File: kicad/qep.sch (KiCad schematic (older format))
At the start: 30 parts, among them J1101 tblock, U1101 SI8660BD, U1102 am26ls32a, U1103 am26ls32a, U1104 SI8660BD

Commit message: placing smmall capacitors and resistors nerar his group
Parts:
- added C1101, C1102, C1103, C1104, C1105, C1106: 100nF, servo:C_0603_1608Metric, symbol servo:Capacitor
- U1102, U1103: footprint Package_SO:SOIC-16_3.9x9.9mm_P1.27mm -> Package_SO:SOIC-16W_5.3x10.2mm_P1.27mm
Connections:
- net labels added: QEP2_A+_H, QEP2_A-_H, QEP2_B+_H, QEP2_B-_H, QEP2_I+_H, QEP2_I-_H, QEP2_S+_H, QEP2_S-_H
- wire segments 185 -> 197

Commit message: touting....
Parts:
- added JP1102: jumper, Jumper:SolderJumper-3_P1.3mm_Open_RoundedPad1.0x1.5mm, symbol servo:Jumper_3_Bridged12
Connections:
- net labels added: Earth
- wire segments 197 -> 202
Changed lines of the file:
@@
 L servo:GNDH #PWR?
 U 1 1 60472C0D
-P 5850 4450
+P 6200 4600
 AR Path="/5DDE8C5E/60472C0D" Ref="#PWR?"  Part="1"
 AR Path="/5E092156/60472C0D" Ref="#PWR0169"  Part="1"
-F 0 "#PWR0169" H 5850 4200 30  0001 C CNN
-F 1 "GNDH" H 5850 4300 20  0000 C CNN
-F 2 "" H 5850 4450 50  0001 C CNN
-F 3 "" H 5850 4450 50  0001 C CNN
-	1    5850 4450
+F 0 "#PWR0169" H 6200 4350 30  0001 C CNN
+F 1 "GNDH" H 6200 4450 20  0000 C CNN
+F 2 "" H 6200 4600 50  0001 C CNN
+F 3 "" H 6200 4600 50  0001 C CNN
+	1    6200 4600
 	-1   0    0    -1
 $EndComp
@@
 	-1   0    0    -1
 $EndComp
+$Comp
+L servo:Jumper_3_Bridged12 JP?
+U 1 1 5E2D8DCE
+P 5850 4550
+AR Path="/5E1BAEAA/5E2D8DCE" Ref="JP?"  Part="1"
+AR Path="/5E21534F/5E2D8DCE" Ref="JP?"  Part="1"
+AR Path="/5E092156/5E2D8DCE" Ref="JP1102"  Part="1"
+F 0 "JP1102" H 5850 4719 39  0000 C CNN
+F 1 "jumper" H 5850 4644 39  0000 C CNN
+F 2 "Jumper:SolderJumper-3_P1.3mm_Open_RoundedPad1.0x1.5mm" H 5650 4350 50  0001 C CNN
+F 3 "~" H 5750 4450 50  0001 C CNN
+	1    5850 4550
+	1    0    0    1
+$EndComp
+Wire Wire Line
+	6050 4550 6200 4550
+Wire Wire Line
+	6200 4550 6200 4600
+$Comp
+L servo:Earth #PWR?
+U 1 1 5E2D8DDD
+P 5500 4600
+AR Path="/5E21534F/5E2D8DDD" Ref="#PWR?"  Part="1"
+AR Path="/5E092156/5E2D8DDD" Ref="#PWR0224"  Part="1"
+F 0 "#PWR0224" H 5500 4350 20  0001 C CNN
+F 1 "Earth" H 5500 4435 39  0000 C CNN
+F 2 "" H 5500 4600 50  0001 C CNN
+F 3 "~" H 5500 4600 50  0001 C CNN
+	1    5500 4600
+	1    0    0    -1
+$EndComp
+Wire Wire Line
+	5650 4550 5500 4550
+Wire Wire Line
+	5500 4550 5500 4600
+Connection ~ 5500 4600
+Wire Wire Line
+	5500 4600 5500 4650
 $EndSCHEMATC

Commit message: moving ethernet connector to right and depopulate 15vh
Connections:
- net labels added: QEP1_A_H, QEP1_A_N_H, QEP1_A_P_H, QEP1_B_H, QEP1_B_N_H, QEP1_B_P_H, QEP1_I_H, QEP1_I_N_H, QEP1_I_P_H, QEP1_S_H, QEP1_S_N_H, QEP1_S_P_H, QEP2_A_H, QEP2_A_N_H, QEP2_A_P_H, QEP2_B_H, QEP2_B_N_H, QEP2_B_P_H, QEP2_I_H, QEP2_I_N_H, QEP2_I_P_H, QEP2_S_H, QEP2_S_N_H, QEP2_S_P_H
- net labels removed: QEP1_A+_H, QEP1_A-_H, QEP1_B+_H, QEP1_B-_H, QEP1_I+_H, QEP1_I-_H, QEP1_S+_H, QEP1_S-_H, QEP2_A+_H, QEP2_A-_H, QEP2_B+_H, QEP2_B-_H, QEP2_I+_H, QEP2_I-_H, QEP2_S+_H, QEP2_S-_H
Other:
- note added: "2x Isolated Idifferential incremental encoder interfase\n5v input A-B-I-S\n"
- note removed: "2x Isolated Idifferential ncremental encoder interfase\n5v input A-B-I-S\n"
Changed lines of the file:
@@
 $EndDescr
 Text Notes 2050 1450 0    197  ~ 39
-2x Isolated Idifferential ncremental encoder  interfase\n5v input A-B-I-S\n
+2x Isolated Idifferential incremental encoder  interfase\n5v input A-B-I-S\n
 Text Notes 3650 1650 0    20   ~ 4
 I left the input for two isolated incremental encoders.\nI left the 4 signals input plus two auxiliary output for eny porpous plus\n the ability to choose between 5 or 15vH
@@
 $EndComp
 Text Label 5400 3650 0    20   ~ 0
-QEP1_B+_H
+QEP1_B_P_H
 Text Label 5400 3750 0    20   ~ 0
-QEP1_B-_H
+QEP1_B_N_H
 Text GLabel 1100 3500 0    50   Input ~ 0
 QEP1_A
@@
 optional one to hi \nor/and one to low
 Text Label 6500 3350 2    20   ~ 0
-QEP2_A+_H
+QEP2_A_P_H
 Text Label 6500 3450 2    20   ~ 0
-QEP2_A-_H
+QEP2_A_N_H
 Text Label 6300 3650 2    20   ~ 0
-QEP2_B+_H
+QEP2_B_P_H
 Text Label 6300 3750 2    20   ~ 0
-QEP2_B-_H
+QEP2_B_N_H
 Text Label 6300 3850 2    20   ~ 0
-QEP2_I+_H
+QEP2_I_P_H
 Text Label 6300 3950 2    20   ~ 0
-QEP2_I-_H
+QEP2_I_N_H
 Text Label 6500 4150 2    20   ~ 0
-QEP2_S+_H
+QEP2_S_P_H
 Text Label 6500 4250 2    20   ~ 0
-QEP2_S-_H
+QEP2_S_N_H
 Text GLabel 10600 3500 2    50   Input ~ 0
 QEP2_A
@@
 optional one to hi \nor/and one to low
 Text Label 5200 3350 0    20   ~ 0
-QEP1_A+_H
+QEP1_A_P_H
 Text Label 5200 3450 0    20   ~ 0
-QEP1_A-_H
+QEP1_A_N_H
 Text Label 5400 3850 0    20   ~ 0
-QEP1_I+_H
+QEP1_I_P_H
 Text Label 5400 3950 0    20   ~ 0
-QEP1_I-_H
+QEP1_I_N_H
 Text Label 5200 4150 0    20   ~ 0
-QEP1_S+_H
+QEP1_S_P_H
 Text Label 5200 4250 0    20   ~ 0
-QEP1_S-_H
+QEP1_S_N_H
 $Comp
 L servo:GND #PWR?
@@
 Wire Wire Line
 	5500 4600 5500 4650
+Text Label 8900 3800 2    20   ~ 0
+QEP2_S_H
+Text Label 8900 3700 2    20   ~ 0
+QEP2_I_H
+Text Label 8900 3600 2    20   ~ 0
+QEP2_B_H
+Text Label 8900 3500 2    20   ~ 0
+QEP2_A_H
+Text Label 2700 3500 0    20   ~ 0
+QEP1_A_H
+Text Label 2700 3600 0    20   ~ 0
+QEP1_B_H
+Text Label 2700 3700 0    20   ~ 0
+QEP1_I_H
+Text Label 2700 3800 0    20   ~ 0
+QEP1_S_H
 $EndSCHEMATC

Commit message: roouting and more routing.... I think 4 layers WONT be enought
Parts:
- removed JP1101: jumper, Jumper:SolderJumper-3_P1.3mm_Open_RoundedPad1.0x1.5mm, symbol servo:Jumper_3_Bridged12
- added JP1101: jumper, servo:SolderJumper-2_P1.3mm_Open_RoundedPad1.0x1.5mm, symbol servo:jumper
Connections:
- net labels added: QEP_5VH
- net labels removed: 15VH
- wire segments 202 -> 201
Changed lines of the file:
@@
 	-1   0    0    -1
 $EndComp
-$Comp
-L servo:Jumper_3_Bridged12 JP?
-U 1 1 603AC069
-P 5850 3000
-AR Path="/5E1BAEAA/603AC069" Ref="JP?"  Part="1"
-AR Path="/5DE3DF56/603AC069" Ref="JP?"  Part="1"
-AR Path="/5E092156/603AC069" Ref="JP1101"  Part="1"
-F 0 "JP1101" H 5850 3169 39  0000 C CNN
-F 1 "jumper" H 5850 3094 39  0000 C CNN
-F 2 "Jumper:SolderJumper-3_P1.3mm_Open_RoundedPad1.0x1.5mm" H 5650 2800 50  0001 C CNN
-F 3 "~" H 5750 2900 50  0001 C CNN
-	1    5850 3000
-	-1   0    0    -1
-$EndComp
-$Comp
-L servo:15VH #PWR?
-U 1 1 603AC070
-P 5550 2950
-AR Path="/5E1BAEAA/603AC070" Ref="#PWR?"  Part="1"
-AR Path="/5DE3DF56/603AC070" Ref="#PWR?"  Part="1"
-AR Path="/5E092156/603AC070" Ref="#PWR0168"  Part="1"
-F 0 "#PWR0168" H 5550 2750 20  0001 C CNN
-F 1 "15VH" H 5550 3107 28  0000 C CNN
-F 2 "" H 5550 2950 50  0001 C CNN
-F 3 "" H 5550 2950 50  0001 C CNN
-	1    5550 2950
-	-1   0    0    -1
-$EndComp
-Wire Wire Line
-	5550 3000 5550 2950
-Wire Wire Line
-	5650 3000 5550 3000
 Wire Wire Line
 	6150 2950 6150 3000
@@
 Wire Wire Line
 	5600 3350 5600 3100
-Wire Wire Line
-	5600 3100 5850 3100
-Connection ~ 5850 3100
 $Comp
 L servo:GNDH #PWR?
@@
 Wire Wire Line
 	6100 3350 6100 3100
-Wire Wire Line
-	5850 3100 6100 3100
 Wire Wire Line
 	6300 3450 7450 3450
@@
 Text Label 2700 3800 0    20   ~ 0
 QEP1_S_H
+$Comp
+L servo:jumper JP?
+U 1 1 5E3094E2
+P 5950 3000
+AR Path="/5DD76B18/5E3094E2" Ref="JP?"  Part="1"
+AR Path="/5E092156/5E3094E2" Ref="JP1101"  Part="1"
+F 0 "JP1101" H 5950 3161 39  0000 C CNN
+F 1 "jumper" H 5950 3086 39  0000 C CNN
+F 2 "servo:SolderJumper-2_P1.3mm_Open_RoundedPad1.0x1.5mm" H 5850 2980 50  0001 C CNN
+F 3 "~" H 5950 3080 50  0001 C CNN
+	1    5950 3000
+	1    0    0    -1
+$EndComp
+Wire Wire Line
+	5600 3100 5850 3100
+Wire Wire Line
+	5850 3000 5850 3100
+Connection ~ 5850 3100
+Wire Wire Line
+	5850 3100 6100 3100
+Text Label 5650 3100 0    20   ~ 0
+QEP_5VH
 $EndSCHEMATC

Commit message: improvement...
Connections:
- net QEP_GND: now reaches J1101.10a (Pin_10a), J1101.10b (Pin_10b), JP1102.2 (C)
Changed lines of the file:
@@
 Text Label 5650 3100 0    20   ~ 0
 QEP_5VH
+Text Label 5950 4400 0    20   ~ 0
+QEP_GND
 $EndSCHEMATC

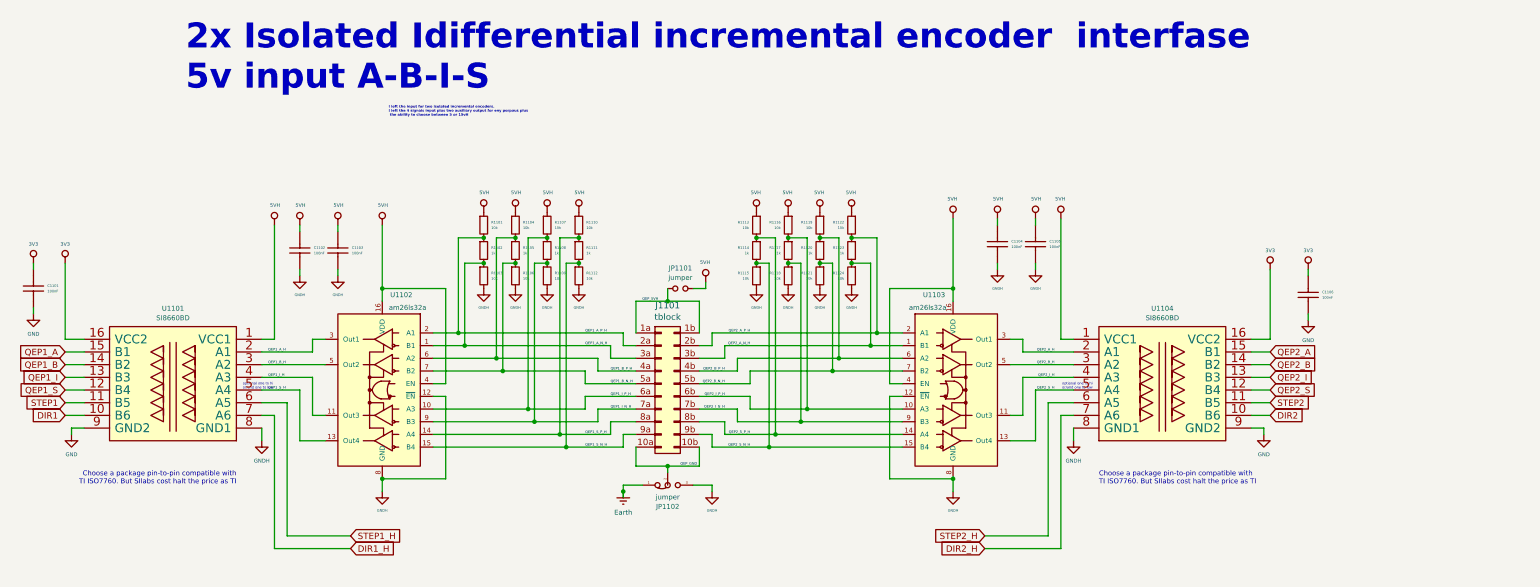
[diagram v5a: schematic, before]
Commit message: change in 5v interface scenario.. remove bridges
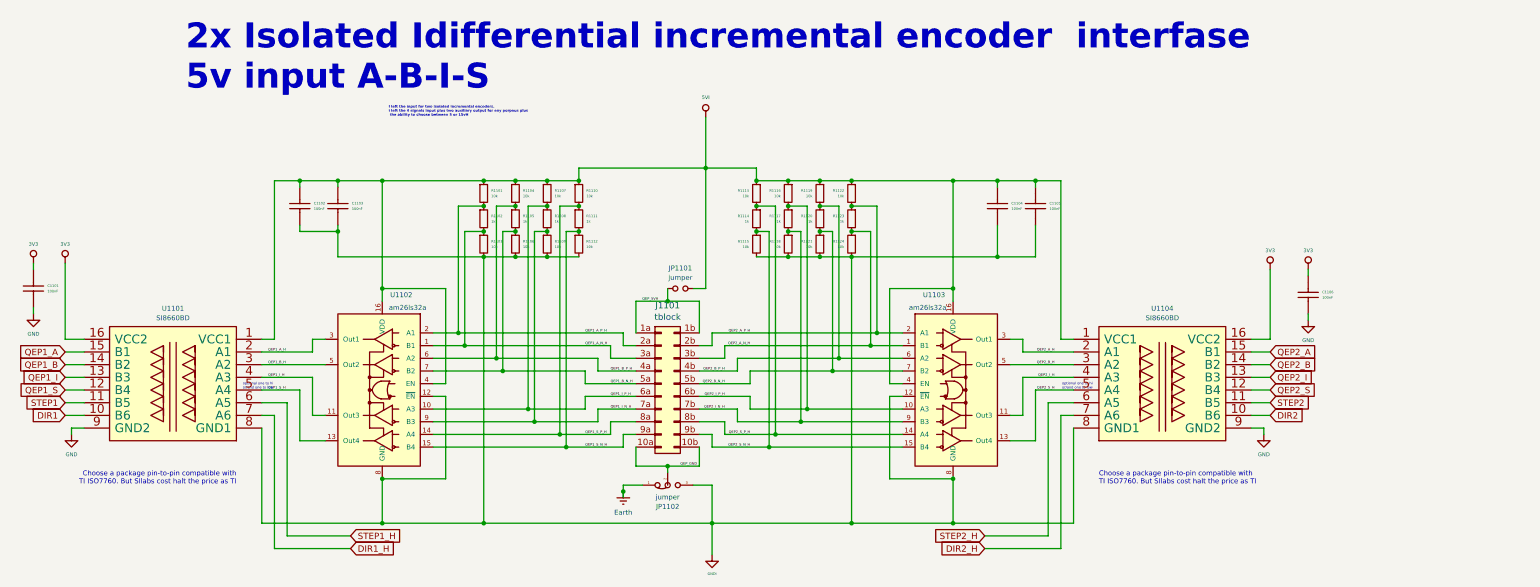
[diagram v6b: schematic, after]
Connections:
- net 5VH renamed 5VI
- net GNDH renamed GNDI
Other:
- moved on the sheet: C1102, C1103, C1104, C1105, R1101, R1102, R1103, R1104, R1105, R1106, R1107, R1108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

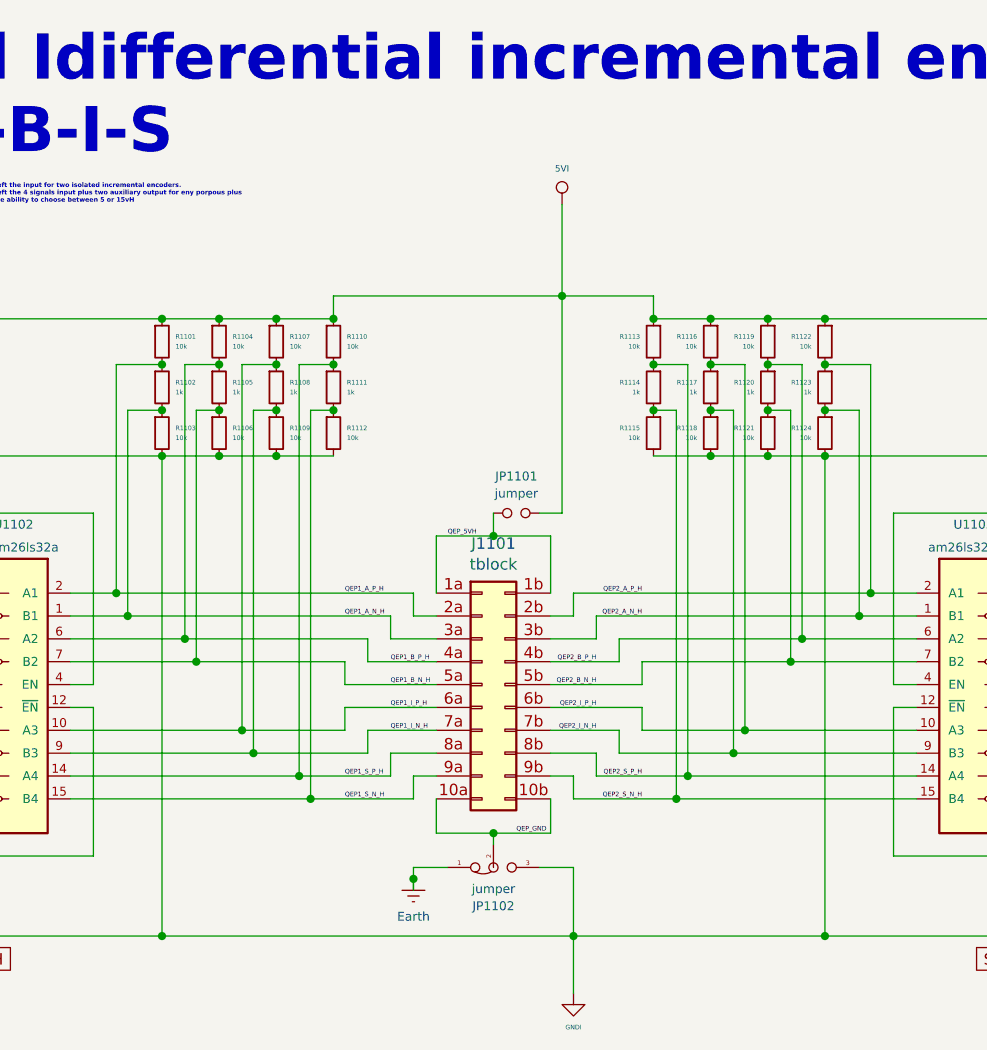
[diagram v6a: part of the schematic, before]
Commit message: added sloted holes everyware
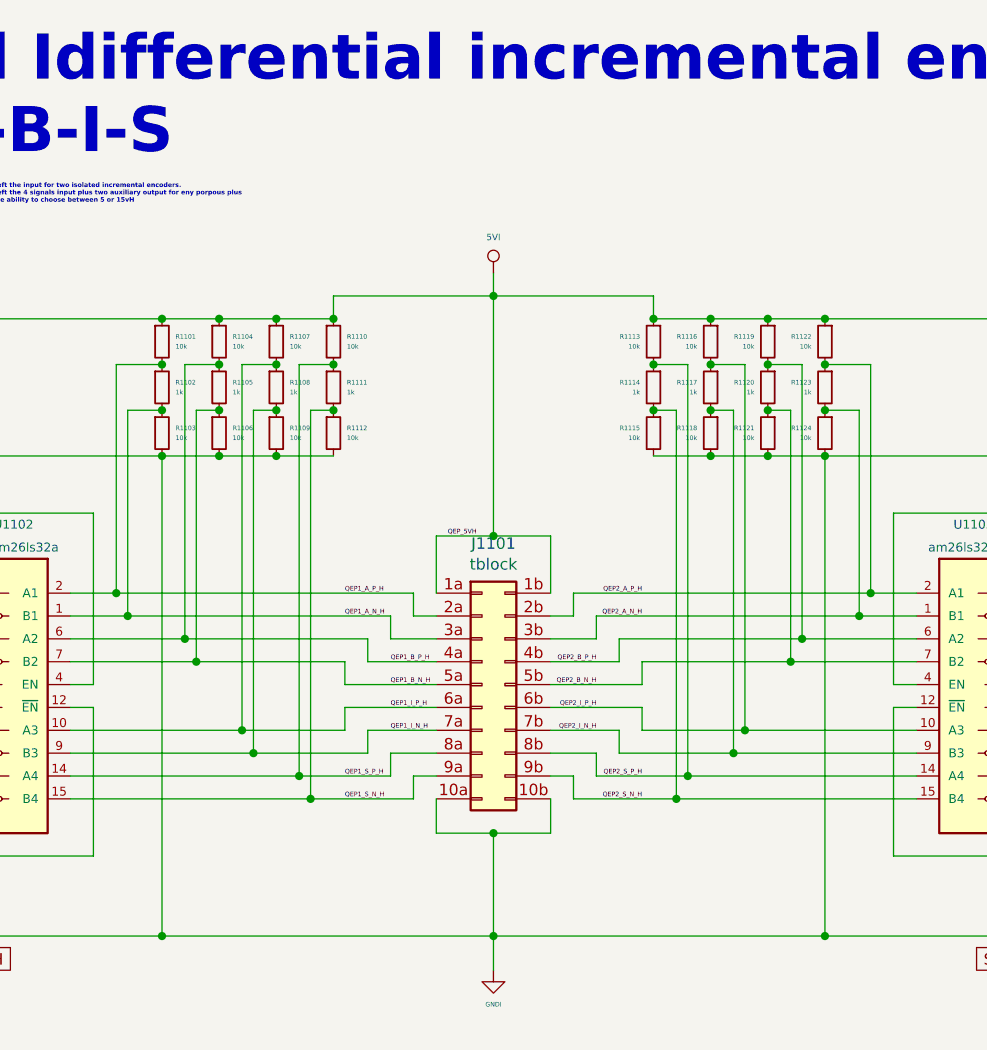
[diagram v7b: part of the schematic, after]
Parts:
- removed JP1101: jumper, servo:SolderJumper-2_P1.3mm_Open_RoundedPad1.0x1.5mm, symbol servo:jumper
- removed JP1102: jumper, Jumper:SolderJumper-3_P1.3mm_Open_RoundedPad1.0x1.5mm, symbol servo:Jumper_3_Bridged12
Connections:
- net QEP_5VH is gone; now on net 5VI: J1101.1a (Pin_1a), J1101.1b (Pin_1b)
- net QEP_GND is gone; now on net GNDI: J1101.10a (Pin_10a), J1101.10b (Pin_10b)
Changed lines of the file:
@@
 Connection ~ 7050 2350
 Wire Wire Line
-	6150 1650 6150 2050
-Wire Wire Line
-	6150 3000 6050 3000
+	5850 1950 5850 2050
 Wire Wire Line
 	5600 3350 5600 3100
-Wire Wire Line
-	5850 4450 5850 4400
 Wire Wire Line
 	8950 2150 8950 3400
@@
 	5600 4250 5600 4400
 Wire Wire Line
-	5600 4400 5850 4400
-Wire Wire Line
 	6100 4400 6100 4250
-Connection ~ 5850 4400
-Wire Wire Line
-	5850 4400 6100 4400
 Wire Wire Line
 	5200 3850 5600 3850
@@
 	-1   0    0    -1
 $EndComp
-$Comp
-L servo:Jumper_3_Bridged12 JP?
-U 1 1 5E2D8DCE
-P 5850 4550
-AR Path="/5E1BAEAA/5E2D8DCE" Ref="JP?"  Part="1"
-AR Path="/5E21534F/5E2D8DCE" Ref="JP?"  Part="1"
-AR Path="/5E092156/5E2D8DCE" Ref="JP1102"  Part="1"
-F 0 "JP1102" H 5850 4719 39  0000 C CNN
-F 1 "jumper" H 5850 4644 39  0000 C CNN
-F 2 "Jumper:SolderJumper-3_P1.3mm_Open_RoundedPad1.0x1.5mm" H 5650 4350 50  0001 C CNN
-F 3 "~" H 5750 4450 50  0001 C CNN
-	1    5850 4550
-	1    0    0    1
-$EndComp
-Wire Wire Line
-	6050 4550 6200 4550
-$Comp
-L servo:Earth #PWR?
-U 1 1 5E2D8DDD
-P 5500 4600
-AR Path="/5E21534F/5E2D8DDD" Ref="#PWR?"  Part="1"
-AR Path="/5E092156/5E2D8DDD" Ref="#PWR0224"  Part="1"
-F 0 "#PWR0224" H 5500 4350 20  0001 C CNN
-F 1 "Earth" H 5500 4435 39  0000 C CNN
-F 2 "" H 5500 4600 50  0001 C CNN
-F 3 "~" H 5500 4600 50  0001 C CNN
-	1    5500 4600
-	1    0    0    -1
-$EndComp
-Wire Wire Line
-	5650 4550 5500 4550
-Wire Wire Line
-	5500 4550 5500 4600
-Connection ~ 5500 4600
-Wire Wire Line
-	5500 4600 5500 4650
 Text Label 8900 3800 2    20   ~ 0
 QEP2_S_H
@@
 Text Label 2700 3800 0    20   ~ 0
 QEP1_S_H
-$Comp
-L servo:jumper JP?
-U 1 1 5E3094E2
-P 5950 3000
-AR Path="/5DD76B18/5E3094E2" Ref="JP?"  Part="1"
-AR Path="/5E092156/5E3094E2" Ref="JP1101"  Part="1"
-F 0 "JP1101" H 5950 3161 39  0000 C CNN
-F 1 "jumper" H 5950 3086 39  0000 C CNN
-F 2 "servo:SolderJumper-2_P1.3mm_Open_RoundedPad1.0x1.5mm" H 5850 2980 50  0001 C CNN
-F 3 "~" H 5950 3080 50  0001 C CNN
-	1    5950 3000
-	1    0    0    -1
-$EndComp
-Wire Wire Line
-	5600 3100 5850 3100
-Wire Wire Line
-	5850 3000 5850 3100
-Connection ~ 5850 3100
-Wire Wire Line
-	5850 3100 6100 3100
 Text Label 5650 3100 0    20   ~ 0
 QEP_5VH
-Text Label 5950 4400 0    20   ~ 0
-QEP_GND
 $Comp
 L servo:5VI #PWR?
 U 1 1 5E3B5024
-P 6150 1650
+P 5850 1950
 AR Path="/5DD76B18/5E3B5024" Ref="#PWR?"  Part="1"
-AR Path="/5E092156/5E3B5024" Ref="#PWR?"  Part="1"
-F 0 "#PWR?" H 6150 1450 20  0001 C CNN
-F 1 "5VI" H 6150 1807 28  0000 C CNN
-F 2 "" H 6150 1650 50  0001 C CNN
-F 3 "" H 6150 1650 50  0001 C CNN
-	1    6150 1650
+AR Path="/5E092156/5E3B5024" Ref="#PWR0143"  Part="1"
+F 0 "#PWR0143" H 5850 1750 20  0001 C CNN
+F 1 "5VI" H 5850 2107 28  0000 C CNN
+F 2 "" H 5850 1950 50  0001 C CNN
+F 3 "" H 5850 1950 50  0001 C CNN
+	1    5850 1950
 	1    0    0    -1
 $EndComp
@@
 	5150 2150 5150 2050
 Wire Wire Line
-	5150 2050 6150 2050
+	5150 2050 5850 2050
 Connection ~ 5150 2150
-Connection ~ 6150 2050
-Wire Wire Line
-	6150 2050 6150 3000
 Wire Wire Line
 	7300 2150 7050 2150
@@
 Wire Wire Line
 	7050 2150 6800 2150
-Wire Wire Line
-	6150 2050 6550 2050
 Wire Wire Line
 	6550 2050 6550 2150
@@
 Connection ~ 7300 2150
 $Comp
-L servo:GNDI #PWR?
+L servo:GNDI #PWR0144
 U 1 1 5E46C528
-P 6200 5100
-F 0 "#PWR?" H 6200 4850 30  0001 C CNN
-F 1 "GNDI" H 6200 4951 20  0000 C CNN
-F 2 "" H 6200 5100 50  0001 C CNN
-F 3 "" H 6200 5100 50  0001 C CNN
-	1    6200 5100
-	1    0    0    -1
-$EndComp
-Wire Wire Line
-	6200 4550 6200 4850
+P 5850 5000
+F 0 "#PWR0144" H 5850 4750 30  0001 C CNN
+F 1 "GNDI" H 5850 4851 20  0000 C CNN
+F 2 "" H 5850 5000 50  0001 C CNN
+F 3 "" H 5850 5000 50  0001 C CNN
+	1    5850 5000
+	1    0    0    -1
+$EndComp
 Wire Wire Line
 	8100 4850 7300 4850
 Wire Wire Line
 	8100 4500 8100 4850
-Connection ~ 6200 4850
 Wire Wire Line
 	3600 4850 4400 4850
@@
 	3600 4500 3600 4850
 Wire Wire Line
-	6200 4850 6200 5100
+	5850 4850 5850 5000
 Wire Wire Line
 	2650 4850 3600 4850
@@
 Connection ~ 4400 4850
 Wire Wire Line
-	4400 4850 6200 4850
+	4400 4850 5850 4850
 Wire Wire Line
 	6550 2750 6800 2750
@@
 Connection ~ 7300 2750
 Connection ~ 7300 4850
-Wire Wire Line
-	7300 4850 6200 4850
 Connection ~ 3600 2150
 Wire Wire Line
@@
 Wire Wire Line
 	8450 2750 8750 2750
+Wire Wire Line
+	5600 4400 5850 4400
+Wire Wire Line
+	5850 4400 5850 4850
+Connection ~ 5850 4400
+Wire Wire Line
+	5850 4400 6100 4400
+Connection ~ 5850 4850
+Wire Wire Line
+	5850 4850 7300 4850
+Wire Wire Line
+	5600 3100 5850 3100
+Connection ~ 5850 2050
+Wire Wire Line
+	5850 2050 5850 3100
+Connection ~ 5850 3100
+Wire Wire Line
+	5850 3100 6100 3100
+Wire Wire Line
+	5850 2050 6550 2050
 $EndSCHEMATC
